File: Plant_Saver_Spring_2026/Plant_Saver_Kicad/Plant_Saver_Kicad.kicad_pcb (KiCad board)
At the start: 2 copper layers, 110 parts, among them J10 DM3D-SF, J11 Test, J2 SBH11-PBPC-D05-ST-BK, J3 SM04B-SRSS-TB, J5 Conn_01x02_Pin, J6 Conn_01x06_Socket, J7 S3B-PH-K-S, J8 54-00284, J9 1.25mm, Q1 G09P02L, Q10 G09P02L, Q11 ISP12DP06NMXTSA1, Q12 G09P02L, Q2 G09P02L, Q3 ISP12DP06NMXTSA1, Q4 G09P02L, Q5 G09P02L, Q6 G09P02L, Q7 G09P02L, Q8 G09P02L, Q9 G09P02L, SW1 Reset, SW2 25336NA, SW3 Boot, SW4 SA72SB0, U1 CDBA140SL-HF, U10 DW03C, U11 CDBA140SL-HF, U12 LP38511TJ-ADJ/NOPB, U13 MCP73833-xxx-UN, U14 MCP6234, U15 MCP73833-xxx-UN, U16 MCP6547T_I_MS, U2 CDBA140SL-HF, U3 CDBA140SL-HF, U4 CDBA140SL-HF, U5 ESP32-WROOM-32E-N16, U9 CDBA140SL-HF

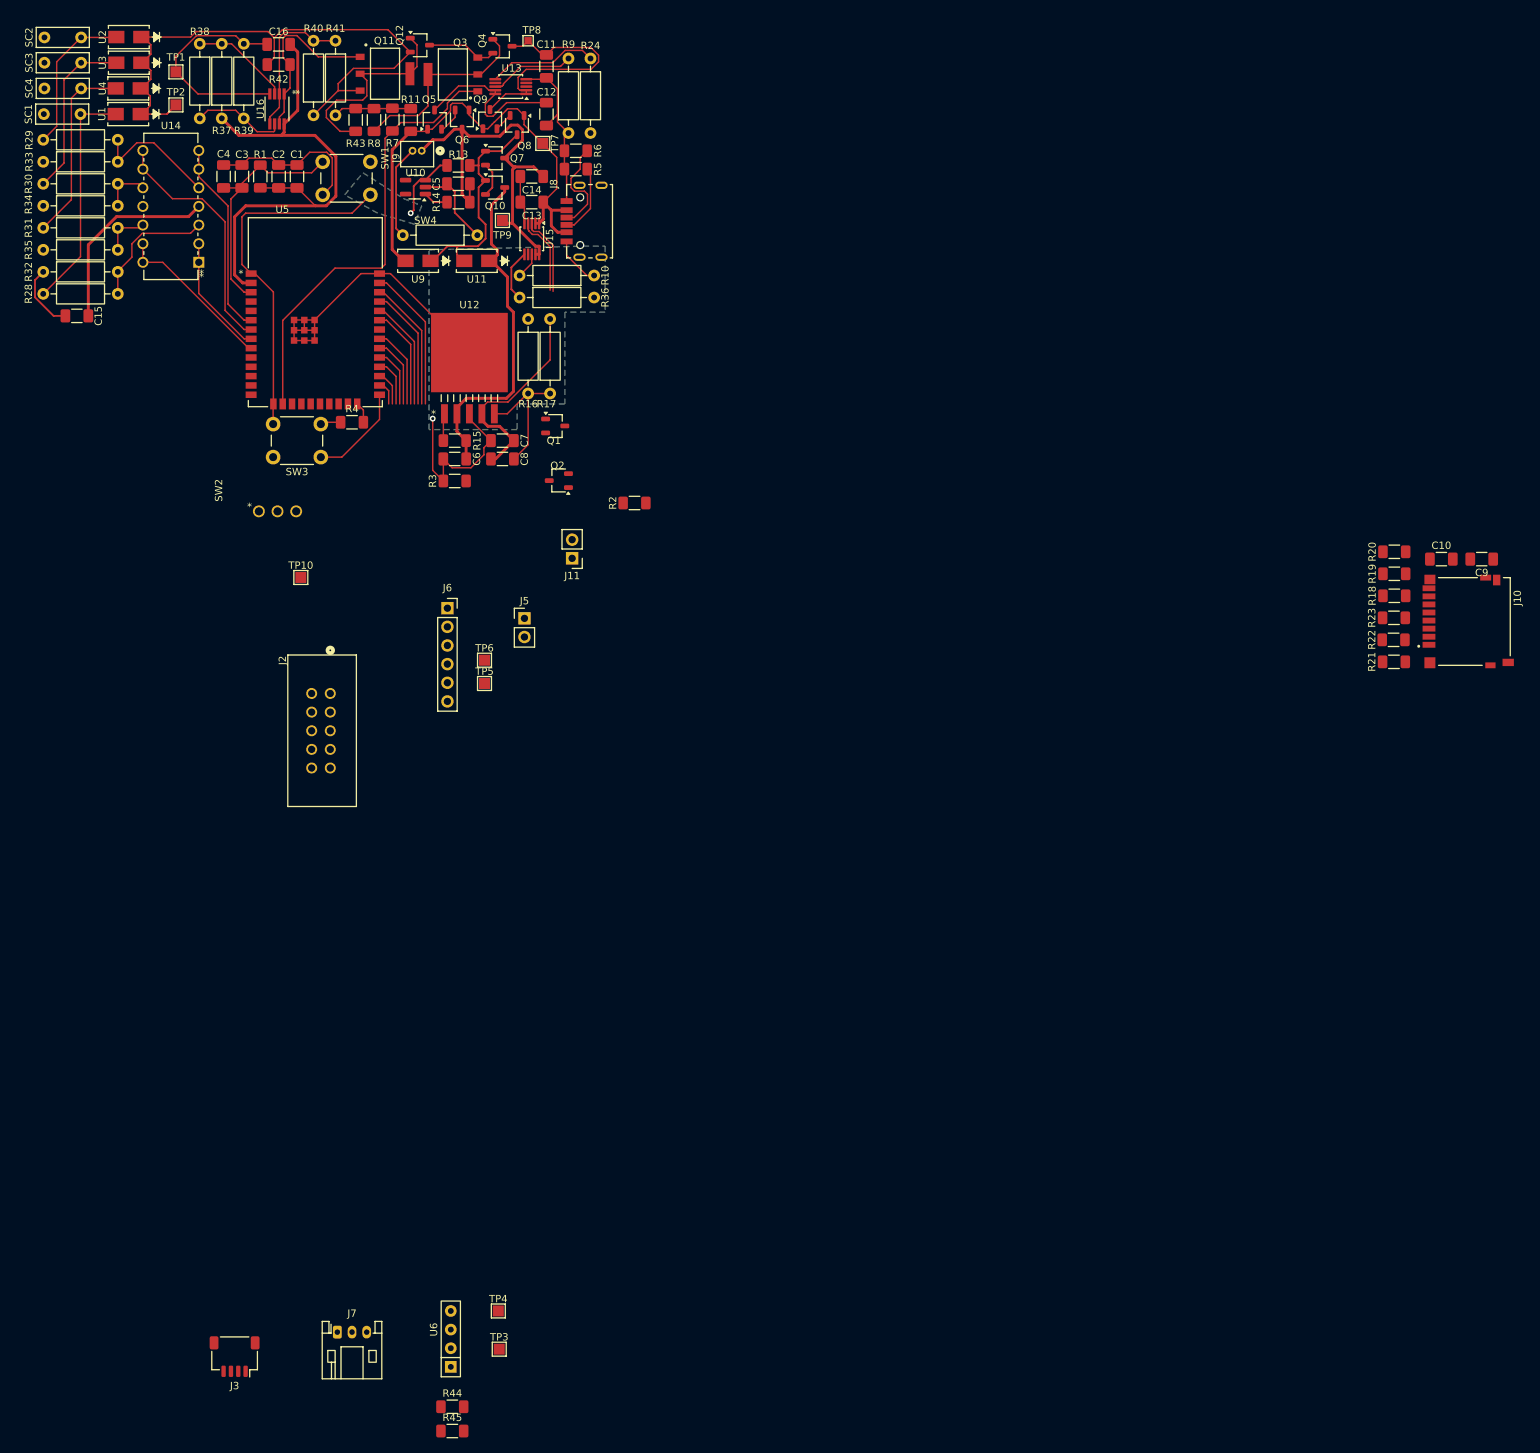
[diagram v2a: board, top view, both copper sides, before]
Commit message: Nearly finished routing
uSD and two I2C connectors remaining.
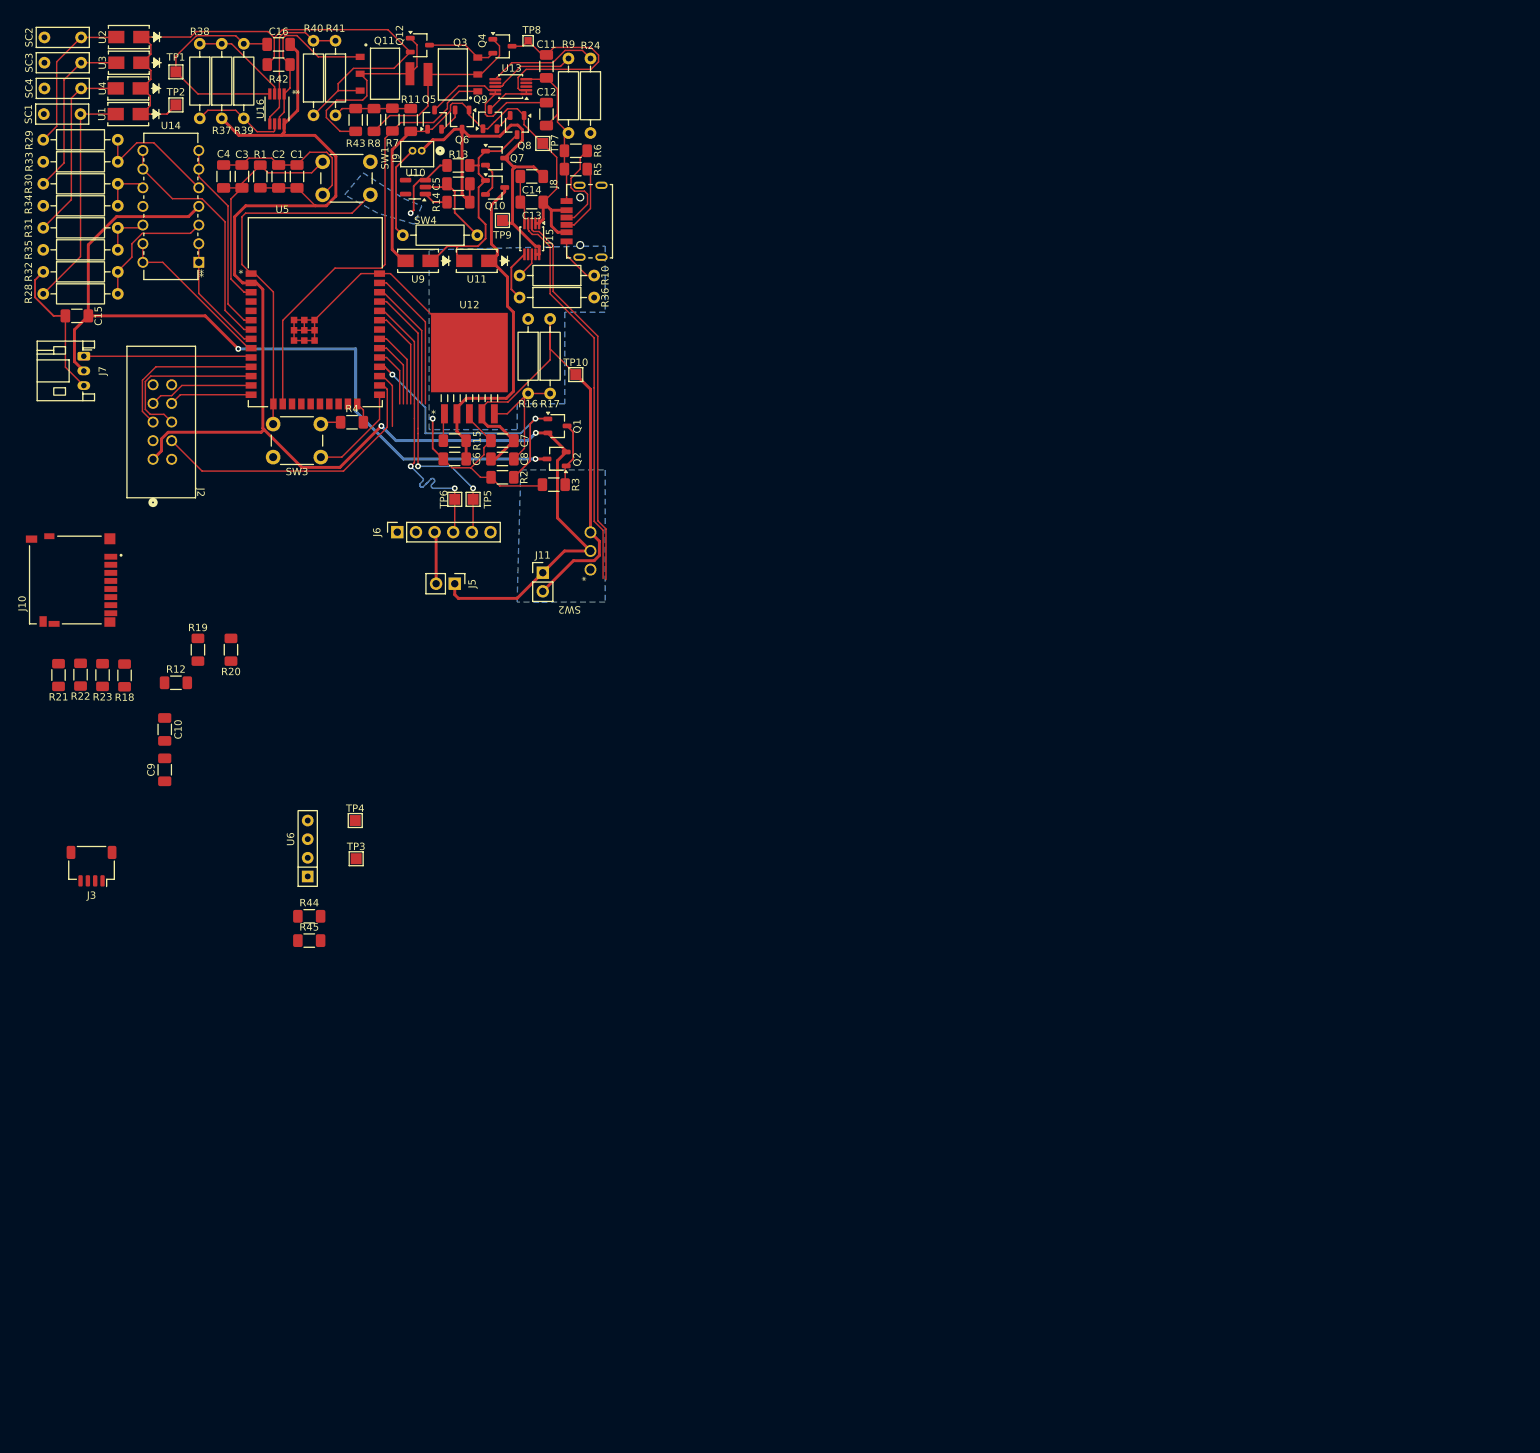
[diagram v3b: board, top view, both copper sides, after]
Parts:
- added R12: 10K, Resistor_SMD:R_1206_3216Metric_Pad1.30x1.75mm_HandSolder, F.Cu at (48.0, 159.0)
- moved R21 182.0 mm to (32.0, 157.9), turned to 90 degrees
- moved C9 181.8 mm to (46.5, 170.9), turned to 90 degrees
- moved J10 179.7 mm to (39.1, 145.0), turned to 90 degrees
- moved R22 179.0 mm to (35.0, 157.9), turned to 90 degrees
- moved R23 176.2 mm to (38.0, 157.9), turned to 90 degrees
- moved C10 175.5 mm to (46.5, 165.4), turned to -90 degrees
- moved R18 173.4 mm to (41.0, 158.0), turned to 90 degrees
- moved R19 163.4 mm to (51.0, 154.5), turned to -90 degrees
- moved R20 159.1 mm to (55.5, 154.5), turned to 90 degrees
- moved J7 137.4 mm to (35.5, 114.5), turned to -90 degrees
- moved TP4 69.6 mm to (72.4, 177.8)
- moved J3 69.6 mm to (36.5, 184.0)
- moved R44 69.6 mm to (66.2, 190.8)
- moved R45 69.6 mm to (66.2, 194.1)
- moved TP3 69.6 mm to (72.6, 183.0)
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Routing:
- net Vbus: track 71.0 -> 196.7 mm, vias 0 -> 2
- net Vperiph: track 27.0 -> 111.5 mm, vias 0 -> 2
- net /Power_And_Charging/Vout: track 29.0 -> 73.8 mm
- net STAT1: track 10.9 -> 53.2 mm
- net STAT2: track 10.8 -> 53.1 mm
- net Error: track 3.35 -> 40.0 mm
- net Periph_EN: track 6.55 -> 38.8 mm, vias 0 -> 2
- net Net-(J6-Pin_4): track 15.0 -> 40.3 mm, vias 0 -> 2
- net Net-(J6-Pin_5): track 16.7 -> 40.0 mm, vias 0 -> 2
- net Aout: track 0.00 -> 22.9 mm
- net Net-(U5-IO27): track 0.00 -> 22.8 mm
- net Net-(U5-IO26): track 0.00 -> 21.9 mm
- net GND: track 240.1 -> 255.6 mm
- net Net-(U5-IO14): track 0.00 -> 14.4 mm
- net Net-(U5-IO12): track 0.00 -> 11.3 mm
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
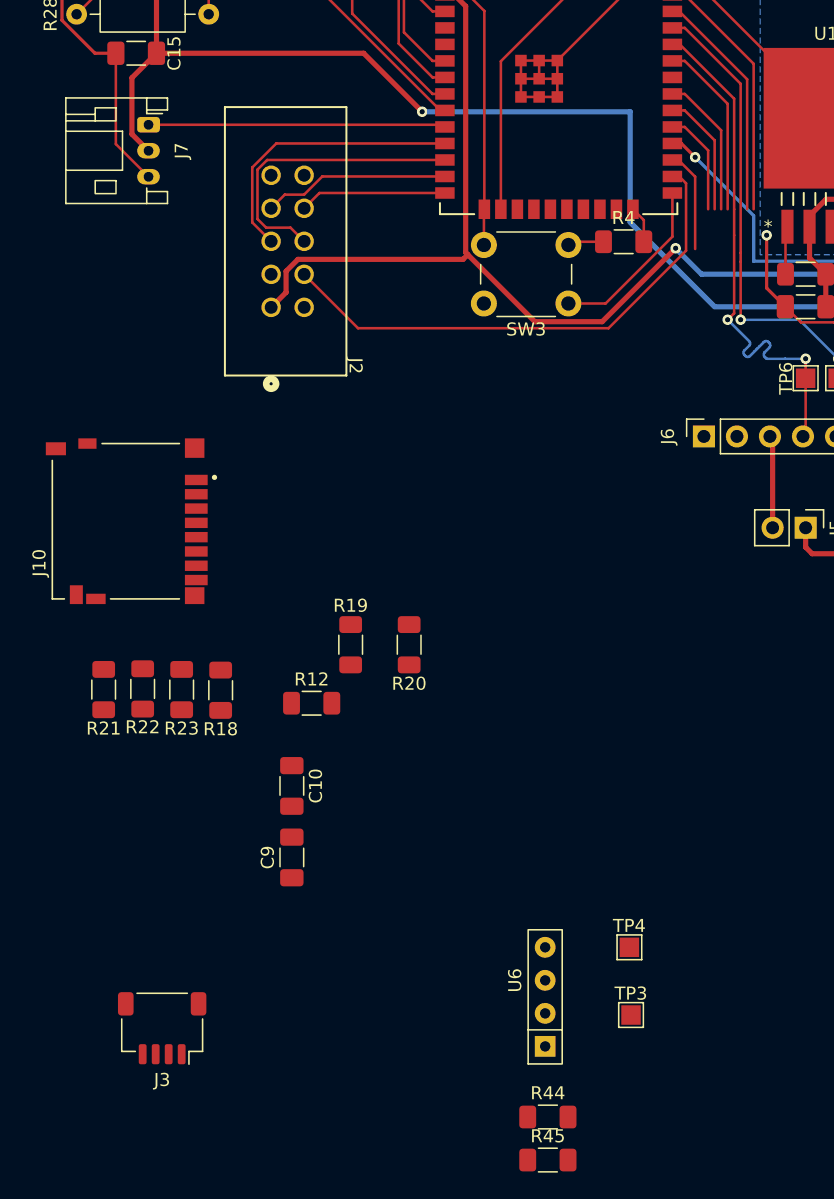
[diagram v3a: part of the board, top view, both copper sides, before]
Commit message: PCB almost finalized
few ground planes left to connect but components are fully connected outside those grounds.
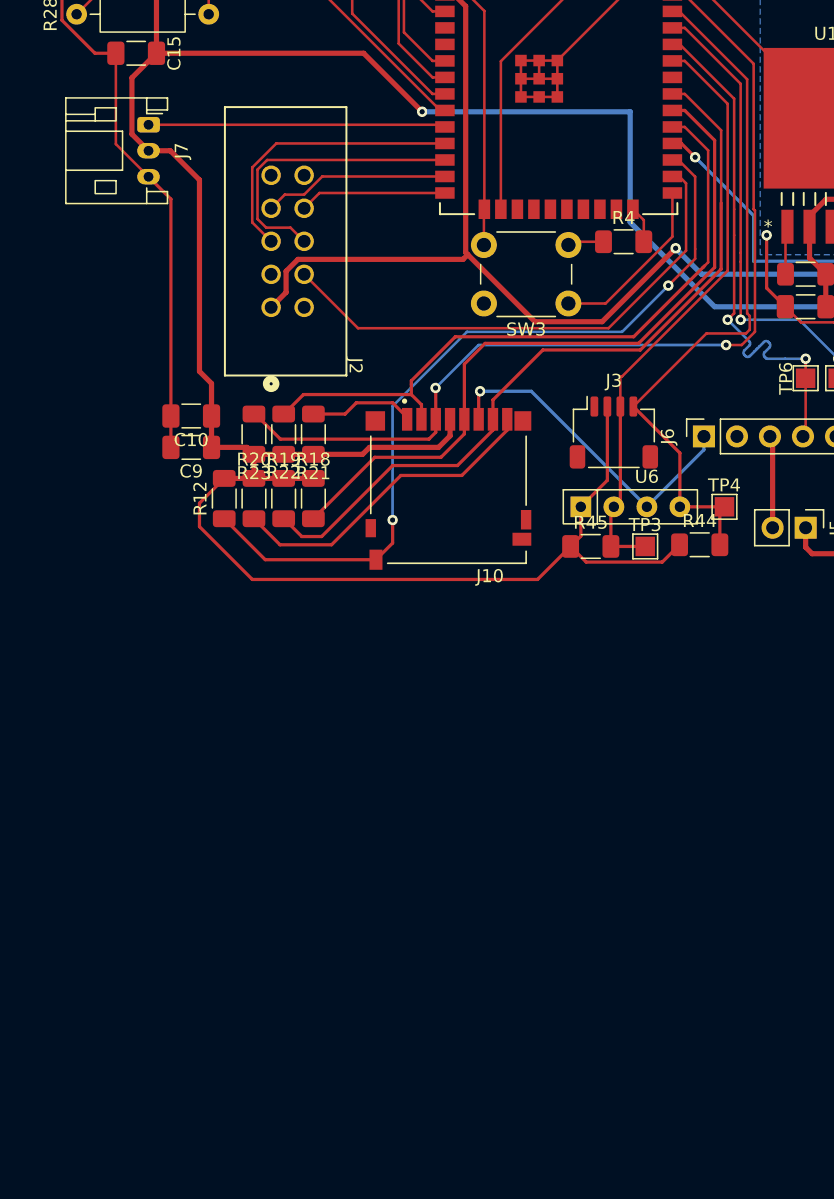
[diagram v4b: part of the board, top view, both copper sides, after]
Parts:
- moved J3 57.5 mm to (71.2, 138.2), turned to 0 degrees
- moved R45 47.3 mm to (69.5, 146.9)
- moved R44 45.5 mm to (77.9, 146.8)
- moved U6 41.6 mm to (68.7, 143.9), turned to 0 degrees
- moved TP3 36.1 mm to (73.7, 146.9)
- moved TP4 34.7 mm to (79.8, 143.9)
- moved C9 32.5 mm to (38.7, 139.3), turned to 180 degrees
- moved C10 29.5 mm to (38.7, 136.9), turned to 180 degrees
- moved R21 25.4 mm to (48.1, 138.3)
- moved R22 22.4 mm to (45.8, 138.3)
- moved J10 21.0 mm to (58.5, 137.2), turned to 180 degrees
- moved R23 20.4 mm to (43.6, 138.3)
- moved R12 17.1 mm to (41.3, 143.3), turned to 90 degrees
- moved R20 16.4 mm to (43.6, 143.3), turned to -90 degrees
- moved R18 16.4 mm to (48.1, 143.3), turned to -90 degrees
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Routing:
- net Vperiph: track 111.5 -> 223.6 mm
- net SPI_MOSI: track 19.6 -> 74.0 mm, vias 0 -> 2
- net uSD_DET: track 7.84 -> 61.9 mm, vias 0 -> 2
- net SPI_MISO: track 11.0 -> 60.2 mm
- net GND: track 255.6 -> 303.2 mm, vias 2 -> 3
- net SPI_CLK: track 9.50 -> 56.0 mm
- net uSD_CS: track 8.03 -> 52.6 mm
- net SCL: track 17.9 -> 54.4 mm
- net SDA: track 13.7 -> 46.1 mm
- net /MicroSD/DAT1: track 0.00 -> 24.8 mm
- net /MicroSD/DAT2: track 0.00 -> 8.19 mm

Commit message: PCB Pre-Check complete
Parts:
- removed the J11 at (98.0, 144.0)
- added J3: Test, Connector_PinHeader_2.54mm:PinHeader_1x02_P2.54mm_Vertical, F.Cu at (91.5, 145.2)
- SW2: value 25336NA -> 1101M2S3AQE2; footprint 25336NA:SWITCH_25336NA_APM -> 1101M2S3AQE2:SPDT-1101M2_CNK
- moved SW2 10.7 mm to (96.1, 137.0)
- renumbered TP9 to BAT1, TP10 to BUS1, C15 to C13, C13 to C14, C14 to C15, TP1 to GND1, J9 to J10, J10 to J11, J3 to J4, J5 to J6, J6 to J7, J7 to J8, J8 to J9, R8 to R10, R9 to R11, R10 to R12, R11 to R13, R13 to R14, R14 to R15, R15 to R16, R16 to R17, R17 to R18, R18 to R19, R19 to R20, R20 to R21, R21 to R22, R22 to R23, R23 to R24, R12 to R25, R24 to R26, R28 to R30, R29 to R31, R30 to R32, R31 to R33, R32 to R34, R33 to R35, R34 to R36, R35 to R37, R36 to R38, R37 to R39, R38 to R40, R39 to R41, R40 to R42, R41 to R43, R42 to R44, R43 to R45, R45 to R5, R44 to R6, R5 to R7, R6 to R8, R7 to R9, TP6 to RX1, TP4 to SCL1, TP3 to SDA1, TP2 to SOL1, TP8 to SOLB1, TP7 to TP1, TP5 to TX1
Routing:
- net STAT2: track 53.1 -> 143.8 mm, vias 0 -> 1
- net STAT1: track 53.2 -> 142.8 mm, vias 0 -> 1
- net GND: track 303.2 -> 320.8 mm
- net Vbus: track 196.7 -> 187.8 mm
- net /Power_And_Charging/Vout: track 73.8 -> 77.1 mm
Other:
- board outline added: 80.5 x 84 mm
- board text added: "FTDI to VBUS"
- board text added: "GND x Vcc TX RX x"
- board text added: "Imeas"
